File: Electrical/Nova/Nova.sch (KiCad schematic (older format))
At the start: 7 parts, among them J2 Conn_01x09_Male, J3 Conn_02x05_Counter_Clockwise, U1 STM32F423RHTx

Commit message: Fixed RF/GPS connector to include additional pins for operation
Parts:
- removed J2: Conn_01x09_Male, Connector_Molex:Molex_PicoBlade_53048-0910_1x09_P1.25mm_Horizontal, symbol Connector:Conn_01x09_Male
- removed J3: Conn_02x05_Counter_Clockwise, Connector_PinSocket_2.54mm:PinSocket_2x05_P2.54mm_Vertical, symbol Connector_Generic:Conn_02x05_Counter_Clockwise
- added J2: Conn_01x13_Male, Connector_Molex:Molex_PicoBlade_53048-1310_1x13_P1.25mm_Horizontal, symbol Connector:Conn_01x13_Male
- added J3: Conn_02x03_Counter_Clockwise, Connector_PinHeader_2.54mm:PinHeader_2x03_P2.54mm_Vertical, symbol Connector_Generic:Conn_02x03_Counter_Clockwise
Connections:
- net labels added: 1PPS, CS, GPSRESET, HRXD1, HRXD2, HTXD1, HTXD2, RFRESET
- net labels removed: CS0, CS1, HGPIO1, HGPIO2, HGPIO3, HGPIO4, HRXD, HTXD
- no-connect marks 1 -> 0
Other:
- moved on the sheet: H1, H2, H3, H4

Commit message: Added Additional Components for Rev 2 Update
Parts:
- removed J3: Conn_02x03_Counter_Clockwise, Connector_PinHeader_2.54mm:PinHeader_2x03_P2.54mm_Vertical, symbol Connector_Generic:Conn_02x03_Counter_Clockwise
- removed U1: STM32F423RHTx, Package_QFP:LQFP-64_10x10mm_P0.5mm, symbol MCU_ST_STM32F4:STM32F423RHTx
- added U1: STM32F411CEUx, Package_DFN_QFN:QFN-48-1EP_7x7mm_P0.5mm_EP5.6x5.6mm, symbol MCU_ST_STM32F4:STM32F411CEUx
- added U8: CD74HC4067M, Package_SO:SOIC-24W_7.5x15.4mm_P1.27mm, symbol 74xx:CD74HC4067M
- added U?: SN74ALVCH16374DGVR, DGV48, symbol SN74ALVCH16374DGVR:SN74ALVCH16374DGVR
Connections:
- net labels added: +3V3, AG_CS, DEMUXCLEAR, DEMUXIN, DEMUXS0, DEMUXS1, DEMUXS2, DEMUXS3, I0, I1, I10, I11, I12, I13, I14, I15, I2, I3, I4, I5, I6, I7, I8, I9, M_CS, NRST
- net labels removed: CLK, CS_AG, CS_M, HGPIO0, IO0, IO1, IO2, IO3, RESET
- wire segments 147 -> 190
- no-connect marks 0 -> 1
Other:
- moved on the sheet: H1, H2, H3, H4

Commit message: More Complete Changes to Rev 2 updated
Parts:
- removed J2: Conn_01x13_Male, Connector_Molex:Molex_PicoBlade_53048-1310_1x13_P1.25mm_Horizontal, symbol Connector:Conn_01x13_Male
- removed U8: CD74HC4067M, Package_SO:SOIC-24W_7.5x15.4mm_P1.27mm, symbol 74xx:CD74HC4067M
- removed U?: SN74ALVCH16374DGVR, DGV48, symbol SN74ALVCH16374DGVR:SN74ALVCH16374DGVR
- added C5: 100nF, Capacitor_SMD:C_0402_1005Metric, symbol pspice:CAP
- added D7, D8: LED, LED_SMD:LED_0402_1005Metric, symbol Device:LED
- added R36: 1k, Resistor_SMD:R_0603_1608Metric, symbol Device:R_US
- added R4: 5.1k, Resistor_SMD:R_0603_1608Metric, symbol Device:R_US
- added R6, R7: 10k, Resistor_SMD:R_0402_1005Metric, symbol Device:R_US
- added SW1, SW2: SW_Push, symbol Switch:SW_Push
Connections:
- net labels added: BOOT0, FSYNC, IMU_CS, IMU_INT, PC13
- net labels removed: 1PPS, AG_CS, CS, DEMUXCLEAR, DEMUXIN, DEMUXS0, DEMUXS1, DEMUXS2, DEMUXS3, DEN, DRDYM, GPSRESET, HRXD1, HRXD2, HTXD1, HTXD2, I0, I1, I10, I11, I12, I13, I14, I15, I2, I3, I4, I5, I6, I7, I8, I9, INT1, INT2, INTM, M_CS, RFRESET, VDDA, VSSA
- wire segments 190 -> 125
- no-connect marks 1 -> 0
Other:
- moved on the sheet: H1, H2, H3, H4, U1

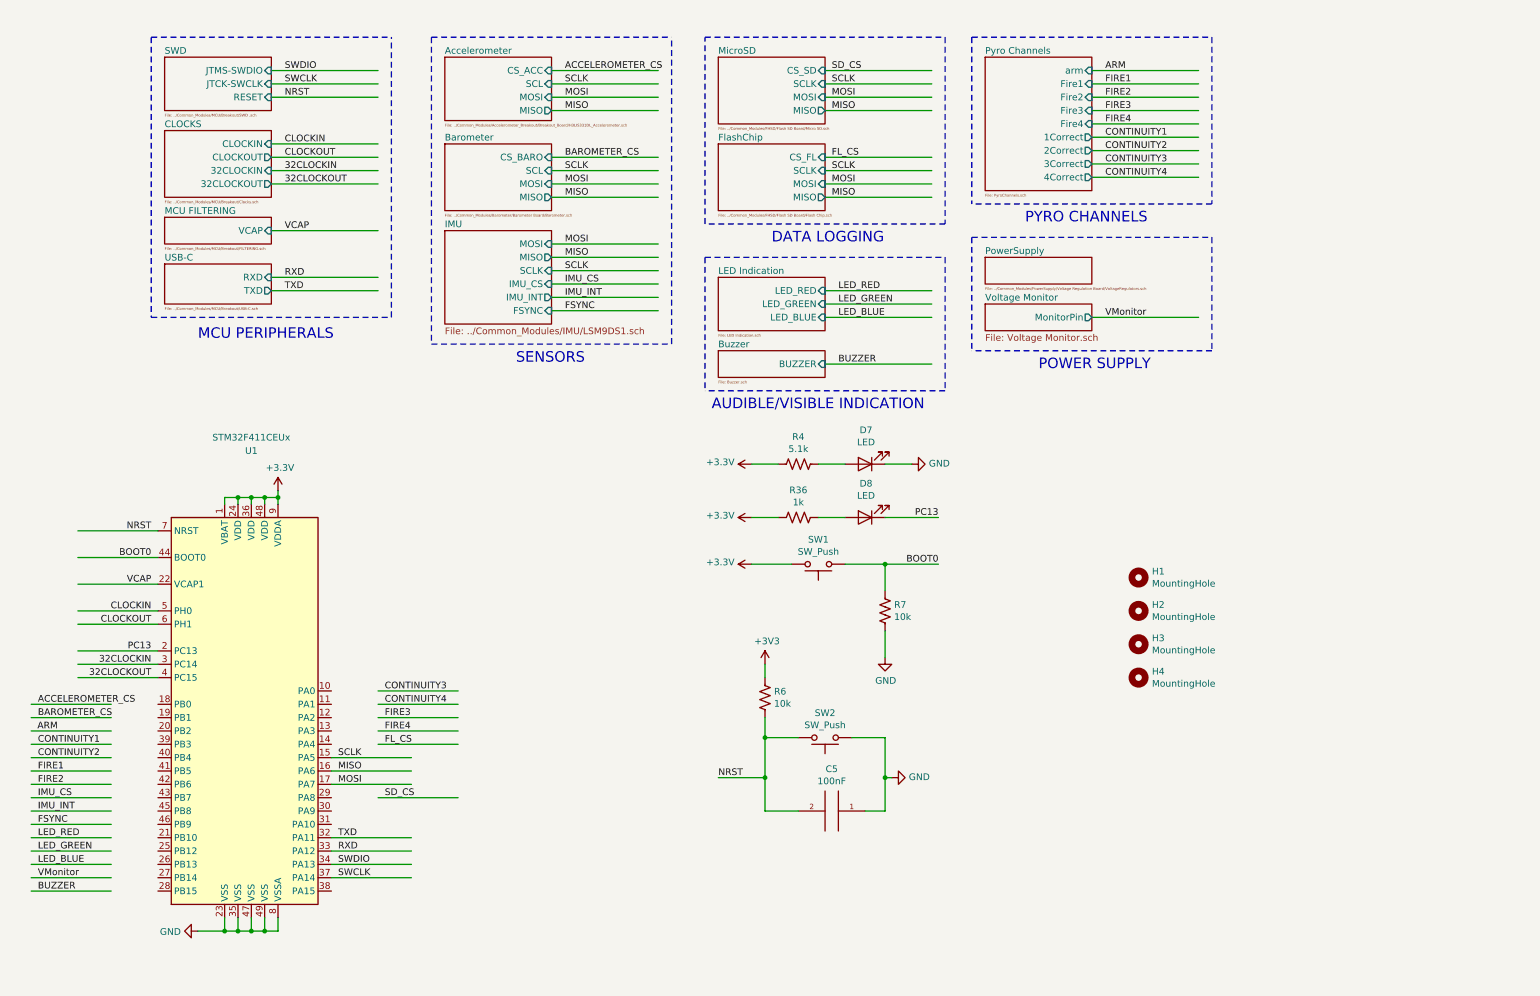
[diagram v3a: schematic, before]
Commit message: Changes to Pyro Logic Circuit
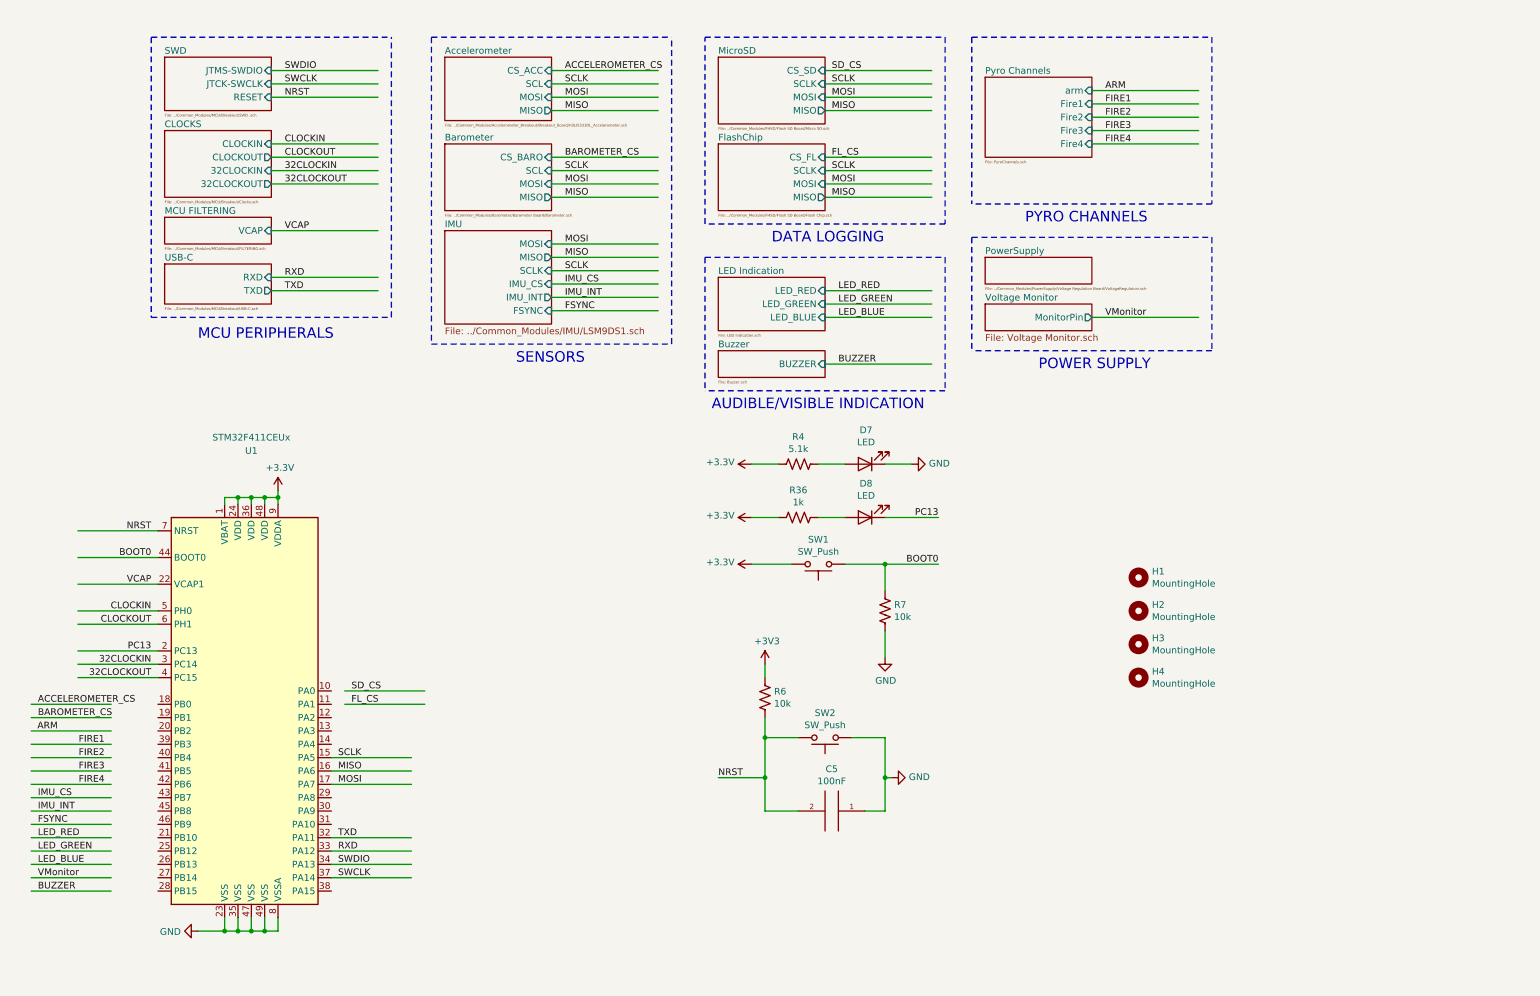
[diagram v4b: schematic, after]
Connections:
- net labels removed: CONTINUITY1, CONTINUITY2, CONTINUITY3, CONTINUITY4
- wire segments 125 -> 117
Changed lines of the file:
@@
 $Descr USLetter 11000 8500
 encoding utf-8
-Sheet 1 15
+Sheet 1 19
 Title ""
 Date ""
@@
 Text Notes 8100 2150 0    79   ~ 0
 PYRO CHANNELS
-Text Label 8700 1300 0    50   ~ 0
+Text Label 8700 1450 0    50   ~ 0
 FIRE3
 $Sheet
-S 7800 900  800  1000
+S 7800 1050 800  600
 U 5F448D4B
 F0 "Pyro Channels" 50
 F1 "PyroChannels.sch" 20
-F2 "arm" I R 8600 1000 50
-F3 "Fire1" I R 8600 1100 50
-F4 "1Correct" O R 8600 1500 50
-F5 "Fire2" I R 8600 1200 50
-F6 "2Correct" O R 8600 1600 50
-F7 "Fire3" I R 8600 1300 50
-F8 "3Correct" O R 8600 1700 50
-F9 "Fire4" I R 8600 1400 50
-F10 "4Correct" O R 8600 1800 50
-$EndSheet
-Text Label 8700 1200 0    50   ~ 0
+F2 "arm" I R 8600 1150 50
+F3 "Fire1" I R 8600 1250 50
+F4 "Fire2" I R 8600 1350 50
+F5 "Fire3" I R 8600 1450 50
+F6 "Fire4" I R 8600 1550 50
+$EndSheet
+Text Label 8700 1350 0    50   ~ 0
 FIRE2
-Text Label 8700 1100 0    50   ~ 0
+Text Label 8700 1250 0    50   ~ 0
 FIRE1
-Text Label 8700 1000 0    50   ~ 0
+Text Label 8700 1150 0    50   ~ 0
 ARM
 Wire Wire Line
-	8600 1000 9400 1000
-Wire Wire Line
-	8600 1100 9400 1100
-Wire Wire Line
-	8600 1200 9400 1200
-Wire Wire Line
-	8600 1500 9400 1500
-Wire Wire Line
-	8600 1600 9400 1600
-Text Label 8700 1500 0    50   ~ 0
-CONTINUITY1
-Text Label 8700 1600 0    50   ~ 0
-CONTINUITY2
-Wire Wire Line
-	8600 1300 9400 1300
-Wire Wire Line
-	8600 1700 9400 1700
-Text Label 8700 1700 0    50   ~ 0
-CONTINUITY3
+	8600 1150 9400 1150
+Wire Wire Line
+	8600 1250 9400 1250
+Wire Wire Line
+	8600 1350 9400 1350
+Wire Wire Line
+	8600 1450 9400 1450
 Wire Notes Line
 	1550 750  3350 750
@@
 	1600 4850 1000 4850
 Wire Wire Line
-	650  6350 1250 6350
-Wire Wire Line
-	650  6150 1250 6150
-Wire Wire Line
-	650  6250 1250 6250
-Wire Wire Line
-	650  6050 1250 6050
-Wire Wire Line
 	1250 7150 650  7150
 Wire Wire Line
@@
 	1250 6750 650  6750
 Wire Wire Line
-	3850 5950 3250 5950
-Wire Wire Line
 	3500 6950 2900 6950
 Wire Wire Line
@@
 	3500 6750 2900 6750
 Wire Wire Line
-	3850 5750 3250 5750
-Wire Wire Line
-	3850 5850 3250 5850
-Wire Wire Line
-	3850 5650 3250 5650
-Wire Wire Line
 	2900 6150 3500 6150
 Wire Wire Line
@@
 Wire Wire Line
 	2900 6350 3500 6350
-Text Label 8700 1400 0    50   ~ 0
+Text Label 8700 1550 0    50   ~ 0
 FIRE4
 Wire Wire Line
-	8600 1400 9400 1400
-Text Label 8700 1800 0    50   ~ 0
-CONTINUITY4
-Wire Wire Line
-	8600 1800 9400 1800
+	8600 1550 9400 1550
 Wire Notes Line
 	9500 750  9500 2000
@@
 Text Label 700  7150 0    50   ~ 0
 BUZZER
-Text Label 700  6050 0    50   ~ 0
-CONTINUITY1
-Text Label 700  6250 0    50   ~ 0
-FIRE1
-Text Label 700  6150 0    50   ~ 0
-CONTINUITY2
-Text Label 700  6350 0    50   ~ 0
-FIRE2
-Text Label 3300 5650 0    50   ~ 0
-CONTINUITY3
-Text Label 3300 5850 0    50   ~ 0
-FIRE3
-Text Label 3300 5750 0    50   ~ 0
-CONTINUITY4
-Text Label 3300 5950 0    50   ~ 0
-FIRE4
 Text Label 850  5950 2    50   ~ 0
 ARM
@@
 Wire Wire Line
 	1250 7050 650  7050
-Text Label 3300 6050 0    50   ~ 0
+Text Label 3050 5750 0    50   ~ 0
 FL_CS
 Wire Wire Line
@@
 	650  5850 1250 5850
 Wire Wire Line
-	3850 6050 3250 6050
-Wire Wire Line
-	3250 6450 3850 6450
+	3600 5750 3000 5750
+Wire Wire Line
+	3000 5650 3600 5650
 Wire Wire Line
 	650  5750 1250 5750
-Text Label 3300 6450 0    50   ~ 0
+Text Label 3050 5650 0    50   ~ 0
 SD_CS
 Text Label 700  5850 0    50   ~ 0
@@
 	2200 4200 2100 4200
 Connection ~ 2200 4200
+Text Label 1200 6350 2    50   ~ 0
+FIRE4
+Text Label 1200 6250 2    50   ~ 0
+FIRE3
+Text Label 1200 6150 2    50   ~ 0
+FIRE2
+Wire Wire Line
+	650  6250 1250 6250
+Wire Wire Line
+	1250 6150 650  6150
+Wire Wire Line
+	1250 6050 650  6050
+Text Label 1200 6050 2    50   ~ 0
+FIRE1
+Wire Wire Line
+	650  6350 1250 6350
 $EndSCHEMATC

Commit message: Began Layout of Nova Rev 2 PCB Updated Version
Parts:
- SW1, SW2: footprint (none) -> NOVA MCU (STM):KSR223GLFG
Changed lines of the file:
@@
 	-1   0    0    1
 $EndComp
-$Comp
-L Device:R_US R36
-U 1 1 61C11E68
-P 6400 4350
-F 0 "R36" V 6195 4350 50  0000 C CNN
-F 1 "1k" V 6286 4350 50  0000 C CNN
-F 2 "Resistor_SMD:R_0603_1608Metric" V 6440 4340 50  0001 C CNN
-F 3 "~" H 6400 4350 50  0001 C CNN
-	1    6400 4350
-	0    1    1    0
-$EndComp
-Wire Wire Line
-	6550 4350 6750 4350
-$Comp
-L power:+3.3V #PWR0124
-U 1 1 61C11E75
-P 6050 4350
-F 0 "#PWR0124" H 6050 4200 50  0001 C CNN
-F 1 "+3.3V" V 6065 4478 50  0000 L CNN
-F 2 "" H 6050 4350 50  0001 C CNN
-F 3 "" H 6050 4350 50  0001 C CNN
-	1    6050 4350
-	0    -1   -1   0
-$EndComp
-Wire Wire Line
-	6050 4350 6250 4350
-$Comp
-L Device:LED D8
-U 1 1 61C11E7D
-P 6900 4350
-F 0 "D8" H 6893 4095 50  0000 C CNN
-F 1 "LED" H 6893 4186 50  0000 C CNN
-F 2 "LED_SMD:LED_0402_1005Metric" H 6900 4350 50  0001 C CNN
-F 3 "~" H 6900 4350 50  0001 C CNN
-	1    6900 4350
-	-1   0    0    1
-$EndComp
-Wire Wire Line
-	7050 4350 7450 4350
 Text Label 1550 5350 2    50   ~ 0
-PC13
-Text Label 7450 4350 2    50   ~ 0
 PC13
 $Comp
@@
 F 0 "SW1" H 6550 4515 50  0000 C CNN
 F 1 "SW_Push" H 6550 4606 50  0000 C CNN
-F 2 "" H 6550 4900 50  0001 C CNN
+F 2 "NOVA MCU (STM):KSR223GLFG" H 6550 4900 50  0001 C CNN
 F 3 "~" H 6550 4900 50  0001 C CNN
 	1    6550 4700
@@
 F 0 "SW2" H 6600 5815 50  0000 C CNN
 F 1 "SW_Push" H 6600 5906 50  0000 C CNN
-F 2 "" H 6600 6200 50  0001 C CNN
+F 2 "NOVA MCU (STM):KSR223GLFG" H 6600 6200 50  0001 C CNN
 F 3 "~" H 6600 6200 50  0001 C CNN
 	1    6600 6000
@@
 Wire Wire Line
 	650  6350 1250 6350
+Text Label 7450 4350 2    50   ~ 0
+PC13
+Wire Wire Line
+	7050 4350 7450 4350
+$Comp
+L Device:LED D8
+U 1 1 61C11E7D
+P 6900 4350
+F 0 "D8" H 6893 4095 50  0000 C CNN
+F 1 "LED" H 6893 4186 50  0000 C CNN
+F 2 "LED_SMD:LED_0402_1005Metric" H 6900 4350 50  0001 C CNN
+F 3 "~" H 6900 4350 50  0001 C CNN
+	1    6900 4350
+	-1   0    0    1
+$EndComp
+Wire Wire Line
+	6050 4350 6250 4350
+$Comp
+L power:+3.3V #PWR0124
+U 1 1 61C11E75
+P 6050 4350
+F 0 "#PWR0124" H 6050 4200 50  0001 C CNN
+F 1 "+3.3V" V 6065 4478 50  0000 L CNN
+F 2 "" H 6050 4350 50  0001 C CNN
+F 3 "" H 6050 4350 50  0001 C CNN
+	1    6050 4350
+	0    -1   -1   0
+$EndComp
+Wire Wire Line
+	6550 4350 6750 4350
+$Comp
+L Device:R_US R36
+U 1 1 61C11E68
+P 6400 4350
+F 0 "R36" V 6195 4350 50  0000 C CNN
+F 1 "1k" V 6286 4350 50  0000 C CNN
+F 2 "Resistor_SMD:R_0603_1608Metric" V 6440 4340 50  0001 C CNN
+F 3 "~" H 6400 4350 50  0001 C CNN
+	1    6400 4350
+	0    1    1    0
+$EndComp
 $EndSCHEMATC
